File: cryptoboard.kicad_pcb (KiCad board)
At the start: 2 copper layers, 53.3 x 50.8 mm, 36 parts, among them J1 USB_A, J2 BOOT, J3 SWD, J4 USR_LEFT, J5 USR_RIGHT, J6 Conn_01x04, SW1 SW_Push, U1 STM32F103C8Tx, U2 LM317_SOT-223-3.3V, Y1 Crystal

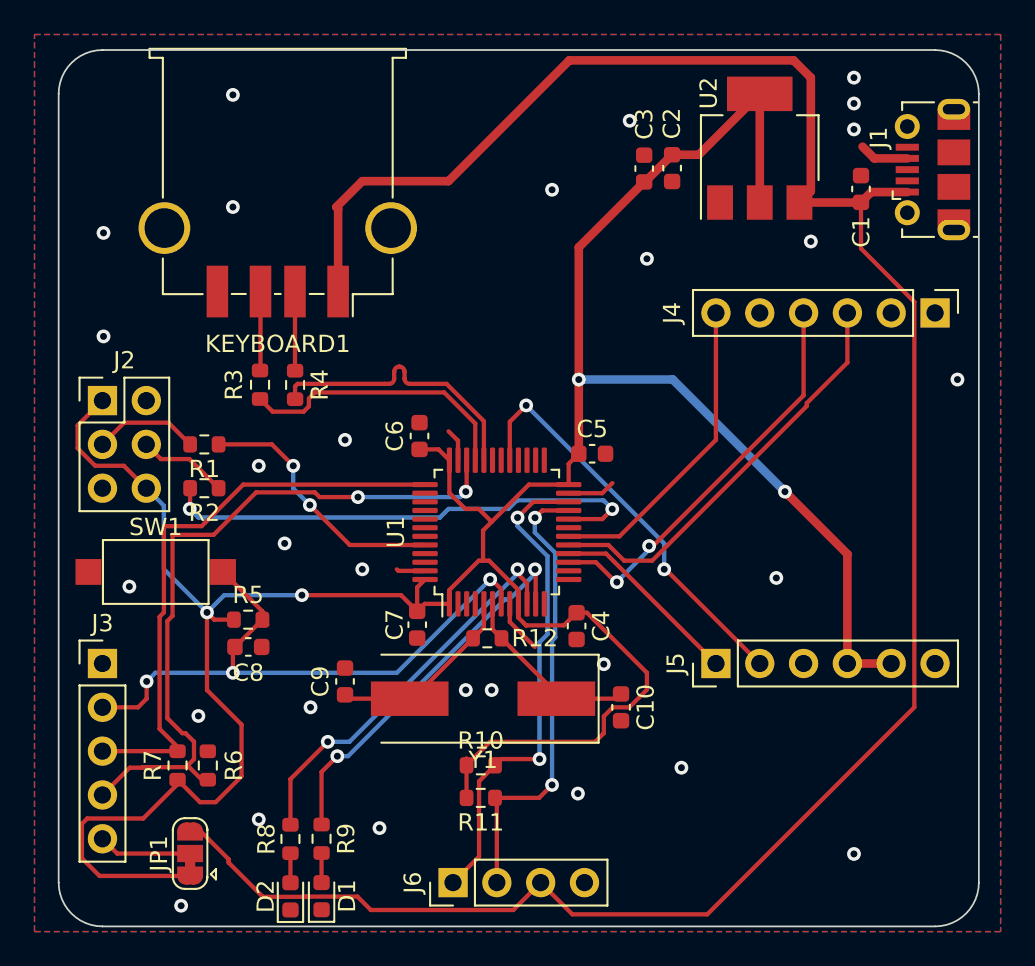
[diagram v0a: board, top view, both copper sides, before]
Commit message: stm32f103 to stm32f107
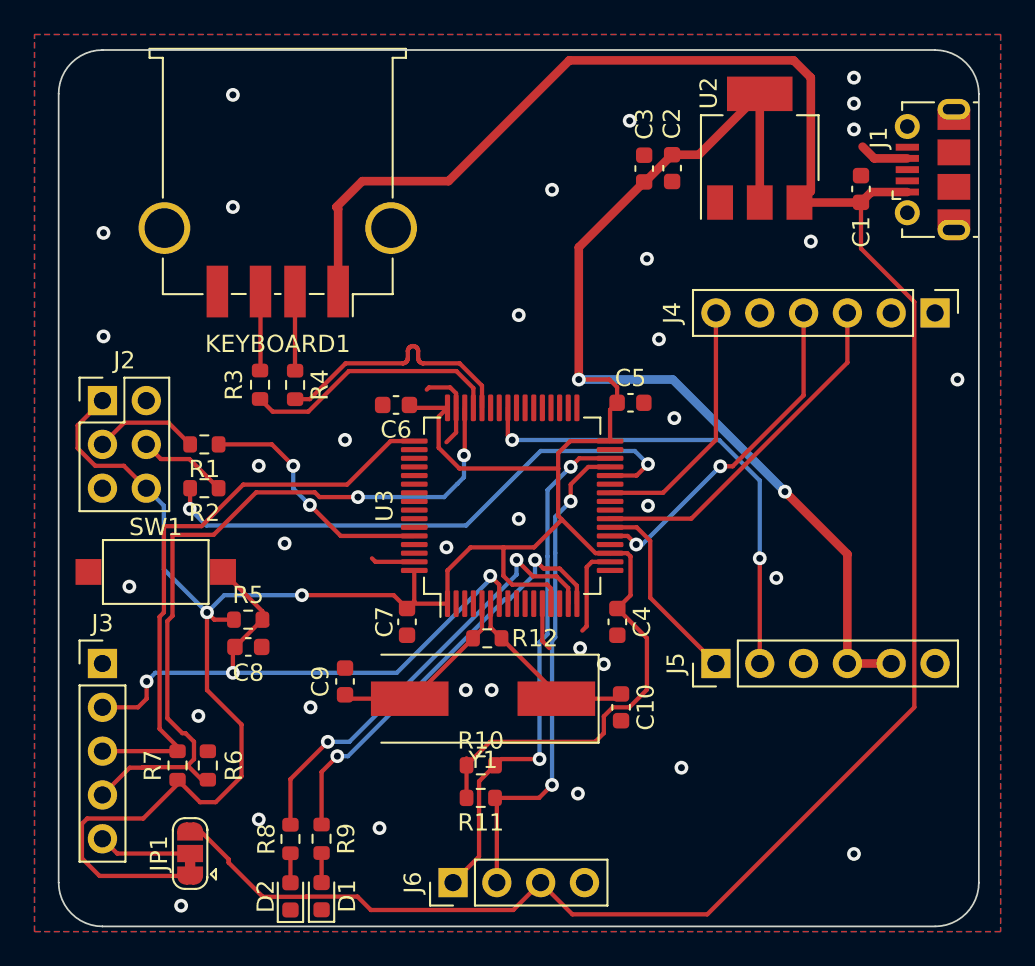
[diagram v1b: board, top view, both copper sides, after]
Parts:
- removed U1: STM32F103C8Tx, Package_QFP:LQFP-48_7x7mm_P0.5mm
- added U3: STM32F107RBTx, Package_QFP:LQFP-64_10x10mm_P0.5mm, F.Cu at (51.7, 51.8)
- moved C5 3.70 mm to (58.5, 45.8)
- moved C4 2.38 mm to (57.8, 58.5)
- moved C6 2.26 mm to (45.0, 46.0), turned to 180 degrees
- moved C7 0.61 mm to (45.6, 58.5)
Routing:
- net +3.3V: track 177.7 -> 192.6 mm
- net GND: track 12.3 -> 18.4 mm, vias 29 -> 35
- net BOOT1: track 29.3 -> 33.4 mm
- net MOSI: track 24.3 -> 20.4 mm
- net ETH_RST: track 24.2 -> 27.9 mm
- net SCLK: track 23.5 -> 19.8 mm
- net INT: track 18.2 -> 14.8 mm
- net LED1: track 23.2 -> 26.1 mm
- net LED2: track 22.5 -> 25.1 mm
- net SWDIO: track 41.7 -> 44.1 mm
- net SCL: track 26.8 -> 29.1 mm
- net SDA: track 28.8 -> 30.7 mm
- net PA11: track 16.3 -> 15.0 mm
- net PA12: track 16.4 -> 15.2 mm
- net BOOT0: track 15.2 -> 14.3 mm
